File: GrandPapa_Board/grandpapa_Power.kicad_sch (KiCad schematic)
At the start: 0 parts

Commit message: Shameless papa copying pt 1
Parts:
- added C?: 0.1uF, Capacitor_SMD:C_0805_2012Metric_Pad1.18x1.45mm_HandSolder, symbol Device:C
- added F?: 500mA, Fuse:Fuse_0805_2012Metric_Pad1.15x1.40mm_HandSolder, symbol Device:Fuse_Small
- added J? (x3): Conn_01x02_Female, Connector_JST:JST_PH_S2B-PH-K_1x02_P2.00mm_Horizontal, symbol Connector:Conn_01x02_Female
- added J?: Conn_01x03_Female, symbol Connector:Conn_01x03_Female
- added R?: 20mR, Resistor_SMD:R_1206_3216Metric_Pad1.30x1.75mm_HandSolder, symbol Device:R_US
- added TP?: TestPoint, Connector_PinHeader_2.54mm:PinHeader_1x01_P2.54mm_Vertical, symbol Connector:TestPoint
- added U? (x2): LM2594M-5.0, Package_SO:SOIC-8_3.9x4.9mm_P1.27mm, symbol Regulator_Switching:LM2594M-5.0
- added U?: INA180A4QDBVRQ1, Package_TO_SOT_SMD:SOT-23-5_HandSoldering, symbol payload2020_custom:INA180
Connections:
- new net: F?.2, R?.2, U?.3 (IN+)
- new net +12V: U?.7 (VIN), U?.7 (VIN)
- new net +5V: C?.2, U?.5 (VS), U?.8 (OUT), U?.8 (OUT)
- new net +BATT: R?.1, TP?.1, U?.4 (IN-)
- new net BATT_CURR_AMP: U?.1 (VO)
- new net GND: C?.1, J?.1 (Pin_1), U?.2 (GND)
- new net UMB_12V: J?.3 (Pin_3)
- no-connect marks 0 -> 1
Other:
- note added: "100V/V"
- note added: "3 LiPO Cells in series"
- note added: "5V always on for MCU and CAN"
- note added: "5V supply to other boards"
- note added: "9-12V"
- note added: "Battery Connectors"
- note added: "Charger IC **Magic**"
- note added: "Main Power Supplies"
- note added: "Umbilical 5/12V"

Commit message: Add power circuits and some PIC stuff, grandpapa lib
5V buck, 3.3V LDO, load switches, current and voltage sensing, some PIC stuff
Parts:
- removed F?: 500mA, Fuse:Fuse_0805_2012Metric_Pad1.15x1.40mm_HandSolder, symbol Device:Fuse_Small
- removed U? (x2): LM2594M-5.0, Package_SO:SOIC-8_3.9x4.9mm_P1.27mm, symbol Regulator_Switching:LM2594M-5.0
- added C? (x3): 0.1uF, symbol Device:C_Small
- added C?: C_Small, symbol Device:C_Small
- added C? (x3): 4.7uF, symbol Device:C_Small
- added C?: 10nF, symbol Device:C_Small
- added C?: 1uF, symbol Device:C_Small
- added C?: 30uF, symbol Device:C_Polarized_Small_US
- added C?: 2.2uF, symbol Device:C_Small
- added C?: 0.33uF, symbol Device:C_Small
- added C?: 100uF 10V, symbol Device:C_Polarized_Small_US
- added C?: 0.1uF, Capacitor_SMD:C_0805_2012Metric_Pad1.18x1.45mm_HandSolder, symbol Device:C
- added D?: 1N914, Diode_THT:D_DO-35_SOD27_P7.62mm_Horizontal, symbol Diode:1N914
- added D?: 1N5818, Diode_THT:D_DO-41_SOD81_P10.16mm_Horizontal, symbol Diode:1N5818
- added F?: 2A, symbol Device:Fuse
- added L?: 30uH, symbol Device:L_Small
- added R? (x3): 500R, Resistor_SMD:R_1206_3216Metric_Pad1.30x1.75mm_HandSolder, symbol Device:R_US
- added R?: 62mR, Resistor_SMD:R_1206_3216Metric_Pad1.30x1.75mm_HandSolder, symbol Device:R_US
- added R?: 100k, Resistor_SMD:R_0805_2012Metric_Pad1.20x1.40mm_HandSolder, symbol Device:R_Small_US
- added R?: 0, symbol Device:R_Small_US
- added R?: 10k, Resistor_SMD:R_0805_2012Metric_Pad1.20x1.40mm_HandSolder, symbol Device:R_Small_US
- added R?: 15.8k, symbol Device:R_Small_US
- added R?: 4.99k, symbol Device:R_Small_US
- added TP?: TestPoint, symbol Connector:TestPoint
- added TP?: TestPoint, Connector_PinHeader_2.54mm:PinHeader_1x01_P2.54mm_Vertical, symbol Connector:TestPoint
- added U? (x3): FPF2124, symbol grandpapa board:FPF2124
- added U?: LT1576IS8-5#TRPBF, symbol grandpapa board:LT1576IS8-5#TRPBF
- added U?: INA180A4QDBVRQ1, Package_TO_SOT_SMD:SOT-23-5_HandSoldering, symbol payload2020_custom:INA180
- added U?: LD2985BM33R, symbol grandpapa board:LD2985BM33R
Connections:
- net +5V: now also C?.1, C?.1, C?.1, C?.2, R?.2, TP?.1, U?.1 (VIN), U?.1 (VIN), U?.1 (VIN), U?.5 (VS)
- net +BATT: now also C?.1, R?.1, U?.2 (VIN)
- net GND: now also J?.1 (Pin_1), C?.1, C?.2, C?.2, C?.2, C?.2, C?.2, C?.2, C?.2, C?.2, C?.2, C?.2, C?.2, C?.2, D?.2 (A), R?.1, R?.2, R?.2, R?.2, R?.2, U?.2 (GND), U?.2 (GND), U?.2 (GND), U?.2 (GND), U?.2 (GND), U?.4 (GND), U?.8 (~{SHDN/SYNC})
- net RAW_BATT: now reaches R?.2, U?.3 (IN+)
- net RAW_BATT: now also F?.2
- net at J?.1 (Pin_1): now also J?.2 (Pin_2)
- net at J?.2 (Pin_2): now also J?.1 (Pin_1)
- net at J?.2 (Pin_2): now also F?.1
- new net: R?.1, U?.4 (ISET) (x3)
- new net: C?.1, D?.1 (K), U?.3 (BOOST)
- new net: C?.1, D?.2 (A), L?.2, R?.1, R?.2, U?.5 (BIAS)
- new net: C?.2, D?.1 (K), L?.1, U?.1 (VSW)
- new net: C?.1, U?.6 (VC)
- new net: R?.1, R?.2, U?.7 (FB/SENSE)
- new net: C?.1, R?.2, U?.3 (IN+), U?.5 (OUT)
- new net: C?.1, U?.4 (BYP)
- new net +3V3: R?.1, TP?.1, U?.4 (IN-)
- new net 3V3_CURR_AMP: U?.1 (VO)
- new net 5V_ALWAYS_ON: C?.1, U?.1 (IN), U?.3 (INHIB)
- new net 5V_LOGGER: C?.1, U?.5 (VOUT)
- new net 5V_MINISENSOR: C?.1, U?.5 (VOUT)
- new net 5V_STRAIN_GUAGE_AMP: C?.1, U?.5 (VOUT)
- new net LOGGER_PWR_EN: U?.3 (ON)
- new net MINISENSOR_PWR_EN: U?.3 (ON)
- new net STRAIN_GUAGE_AMP_PWR_EN: U?.3 (ON)
- new net V_SENSE: R?.1, R?.2
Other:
- note added: "1.09-1.46V output"
- note added: "12-16V"
- note added: "20mR * 100V/V * Imax = 5V Imax = 2.5A"
- note added: "3.3V LDO ALWAYS ON: PIC SUPPLY VOLTAGE"
- note added: "5V ALWAYS ON BUCK REGULATOR"
- note added: "62mR * 100V/V * Imax = 5V Imax = 0.81A"
- note added: "ALUMINUM CAP"
- note added: "ALWAYS ON"
- note added: "ENABLE AT >1.3V"
- note added: "ILIM = 460/RSET = 460/500R = 0.92A CURRENT LIMIT THROUGH EACH OF THE SWITCHES"
- note added: "IMAX = 1.25A"
- note added: "IMAX = 150mA"
- note added: "INPUT CAP CAN BE BETWEEN 15uF - 50uF"
- note added: "L = 60uH FOR LOADS BETWEEN 0.6A AND 1A"
- note added: "PERIPHERAL BOARD LOAD SWITCHES"
- note added: "TANTALLUM CAP"
- note added: "Voltage Sensing"
- note removed: "5V always on for MCU and CAN"
- note removed: "5V supply to other boards"
- moved on the sheet: C?, R?, TP?, U?

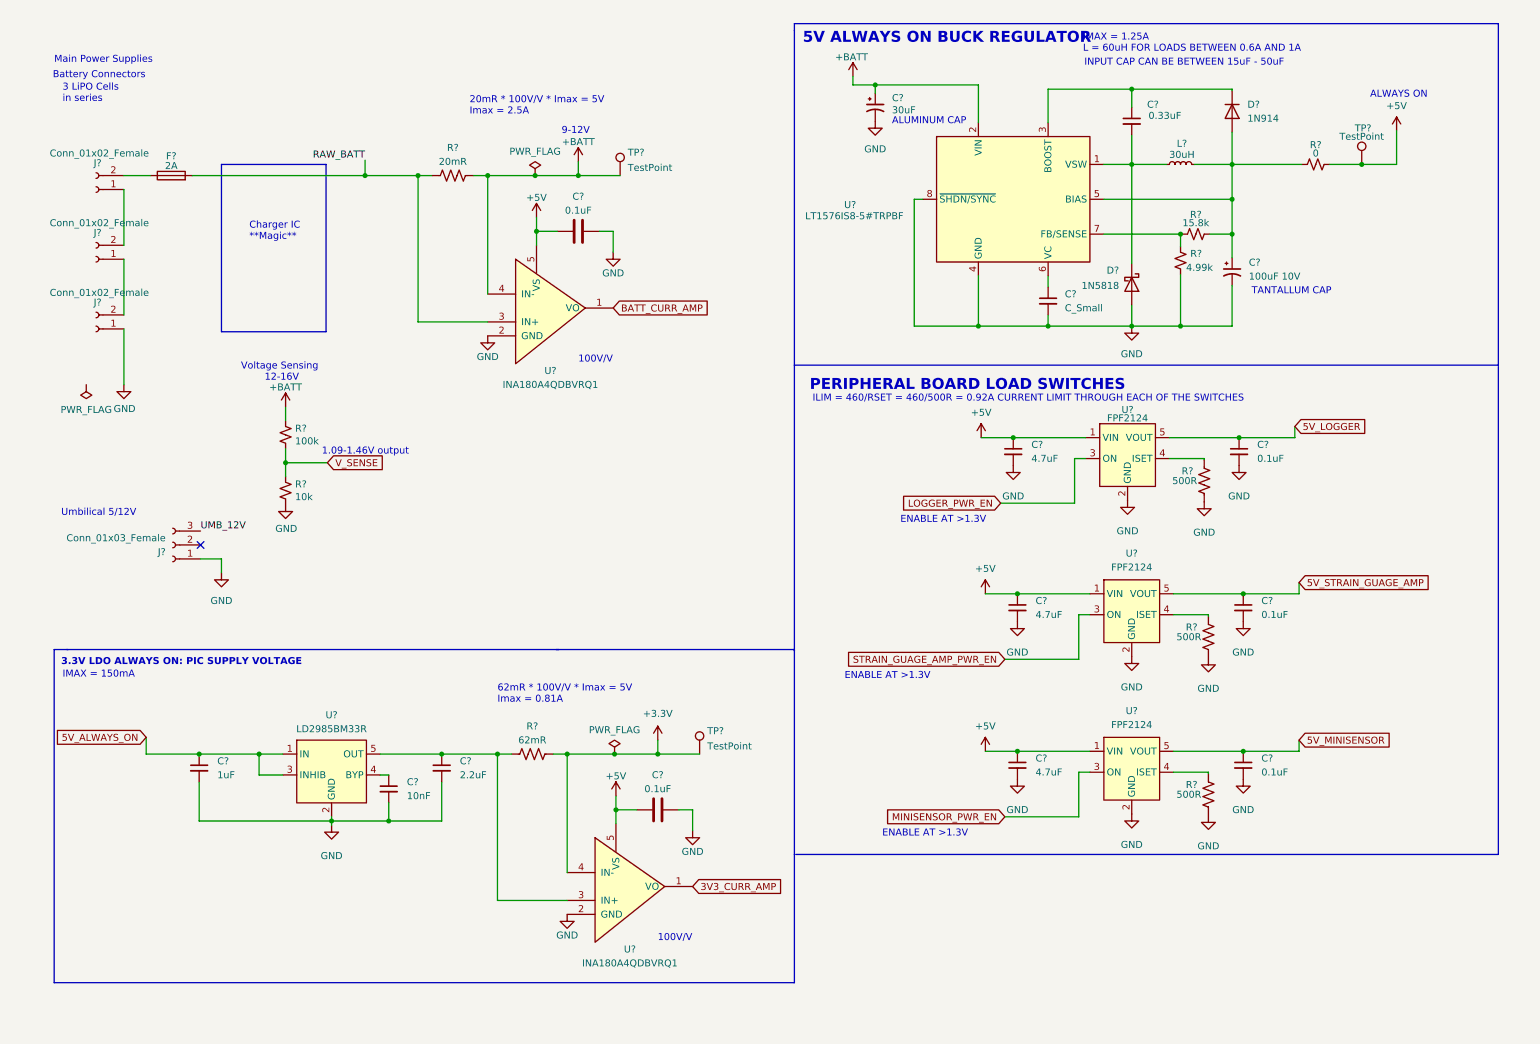
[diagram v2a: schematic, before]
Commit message: Add missing capacitor value, annotate symbols
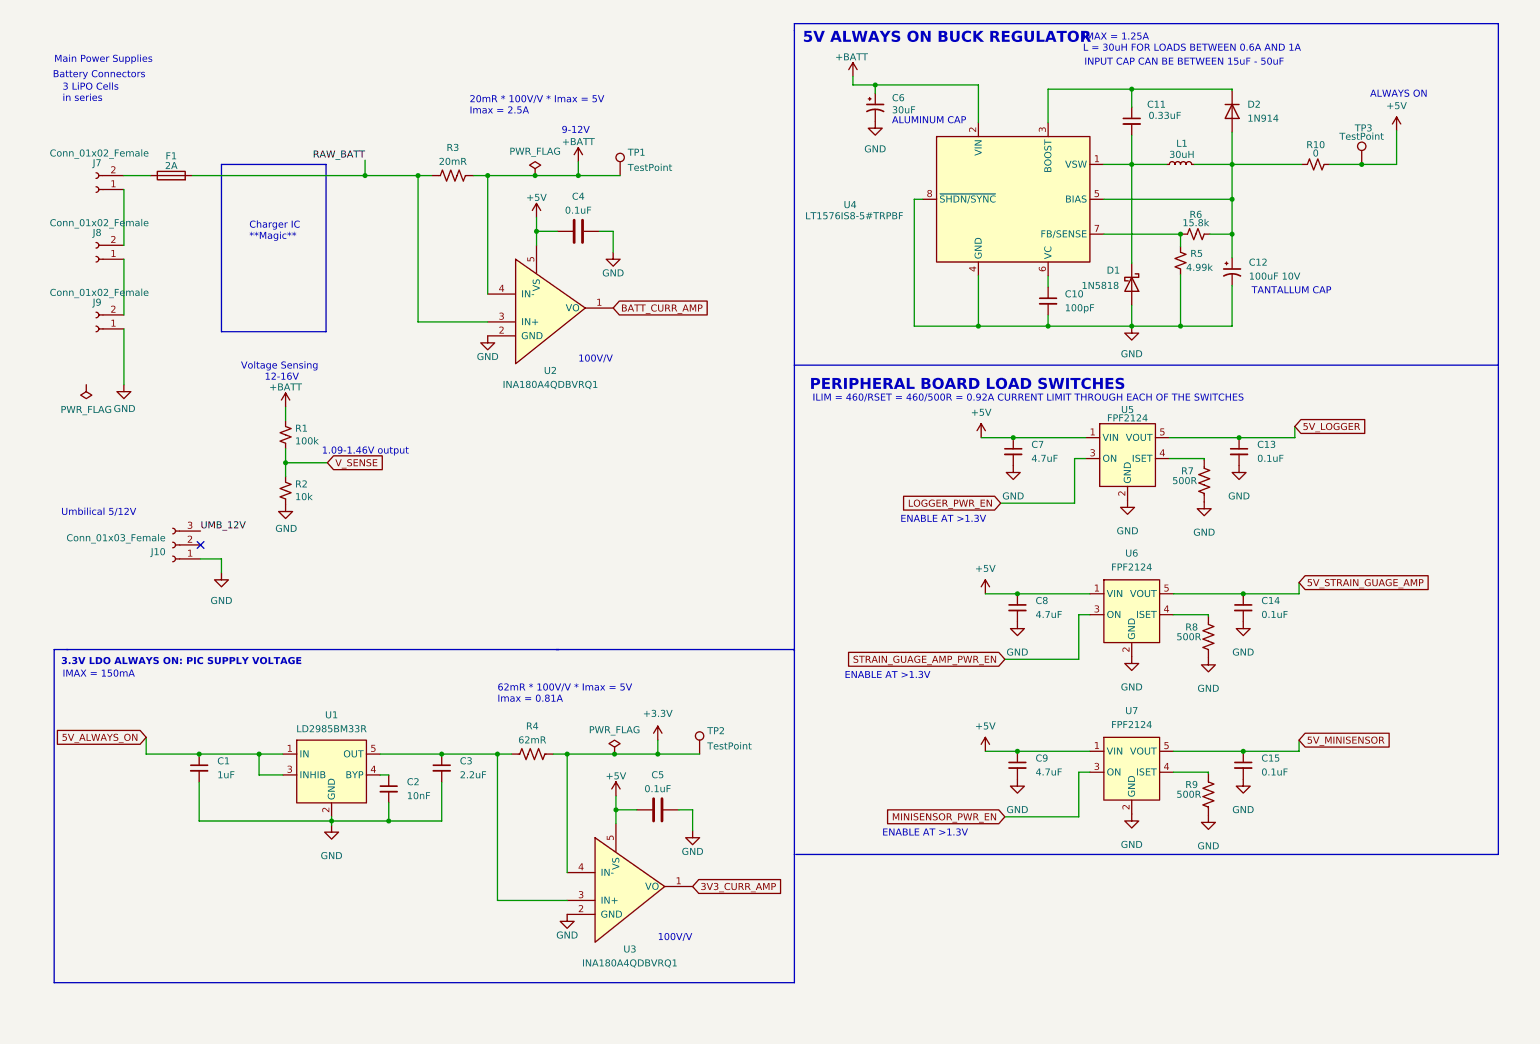
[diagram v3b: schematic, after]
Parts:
- C10: renamed from C?; value C_Small -> 100pF
- gave numbers to parts that had none: 42
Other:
- note added: "L = 30uH FOR LOADS BETWEEN 0.6A AND 1A"
- note removed: "L = 60uH FOR LOADS BETWEEN 0.6A AND 1A"

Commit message: Add motor current sense amp and board output connections
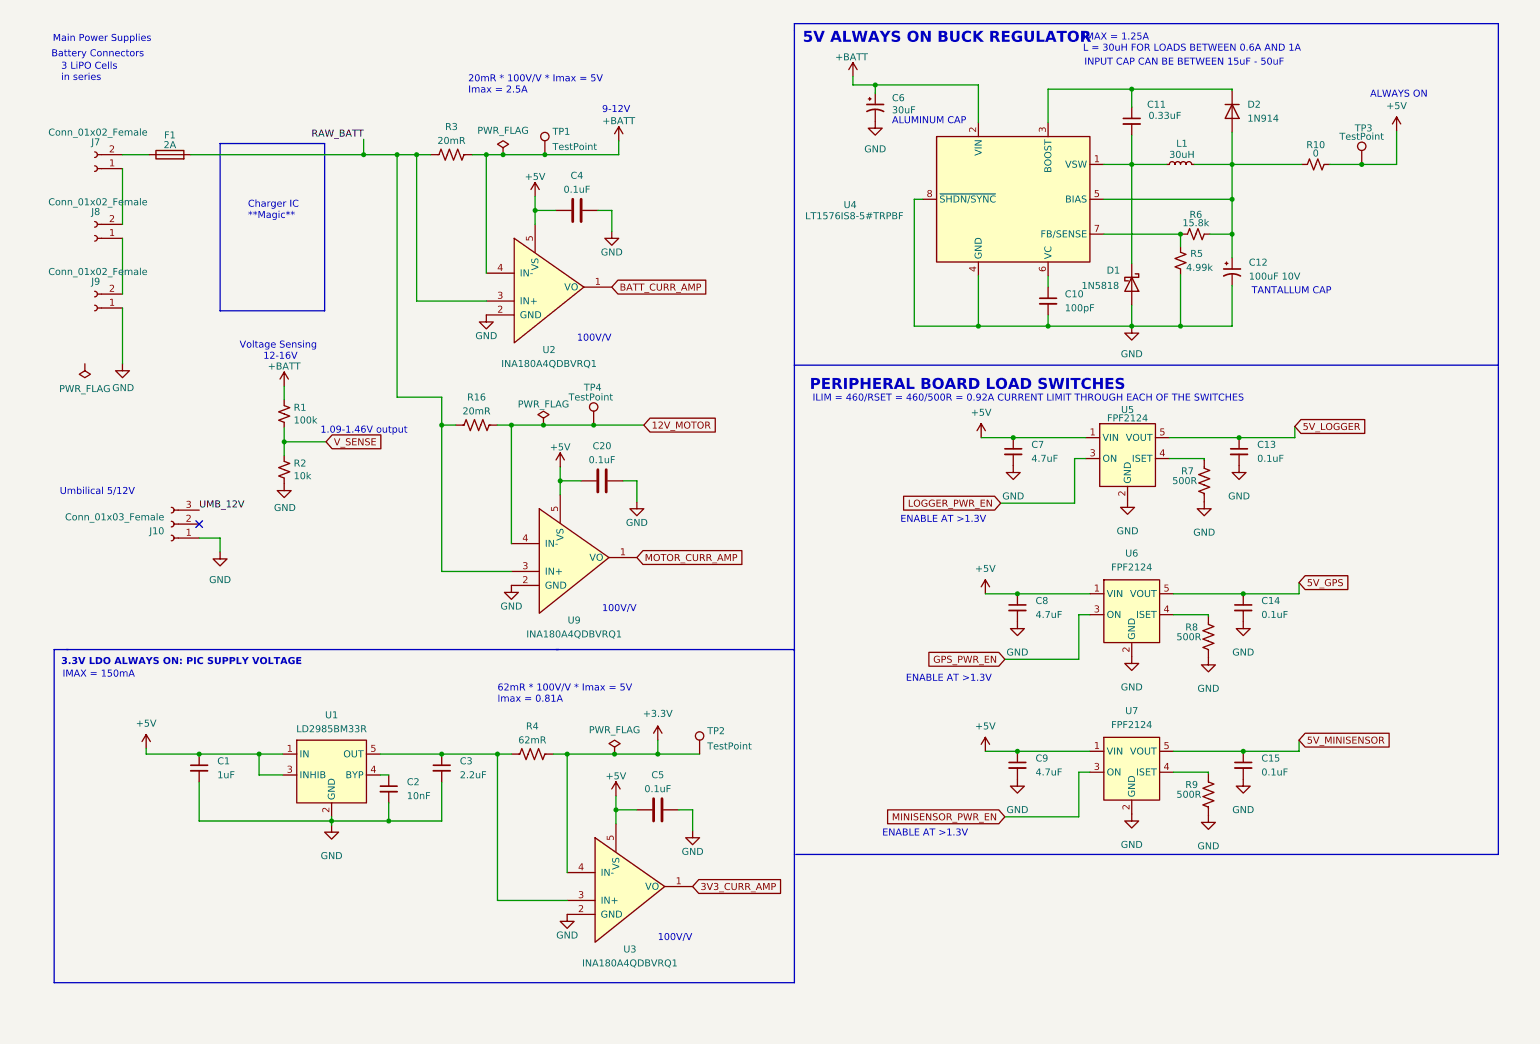
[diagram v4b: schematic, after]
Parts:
- added C20: 0.1uF, Capacitor_SMD:C_0805_2012Metric_Pad1.18x1.45mm_HandSolder, symbol Device:C
- added R16: 20mR, Resistor_SMD:R_1206_3216Metric_Pad1.30x1.75mm_HandSolder, symbol Device:R_US
- added TP4: TestPoint, Connector_PinHeader_2.54mm:PinHeader_1x01_P2.54mm_Vertical, symbol Connector:TestPoint
- added U9: INA180A4QDBVRQ1, Package_TO_SOT_SMD:SOT-23-5_HandSoldering, symbol payload2020_custom:INA180
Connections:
- net 5V_ALWAYS_ON is gone; now on net +5V: C1.1, U1.1 (IN), U1.3 (INHIB)
- net +5V: now also C20.2, U9.5 (VS)
- net GND: now also C20.1, U9.2 (GND)
- net RAW_BATT: now also R16.2, U9.3 (IN+)
- net 5V_STRAIN_GUAGE_AMP renamed 5V_GPS
- net STRAIN_GUAGE_AMP_PWR_EN renamed GPS_PWR_EN
- new net 12V_MOTOR: R16.1, TP4.1, U9.4 (IN-)
- new net MOTOR_CURR_AMP: U9.1 (VO)
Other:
- moved on the sheet: C4, F1, J10, J7, J8, J9, R1, R2, R3, TP1, U2

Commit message: Add INA180 to symbol lib, update 5v switch labels
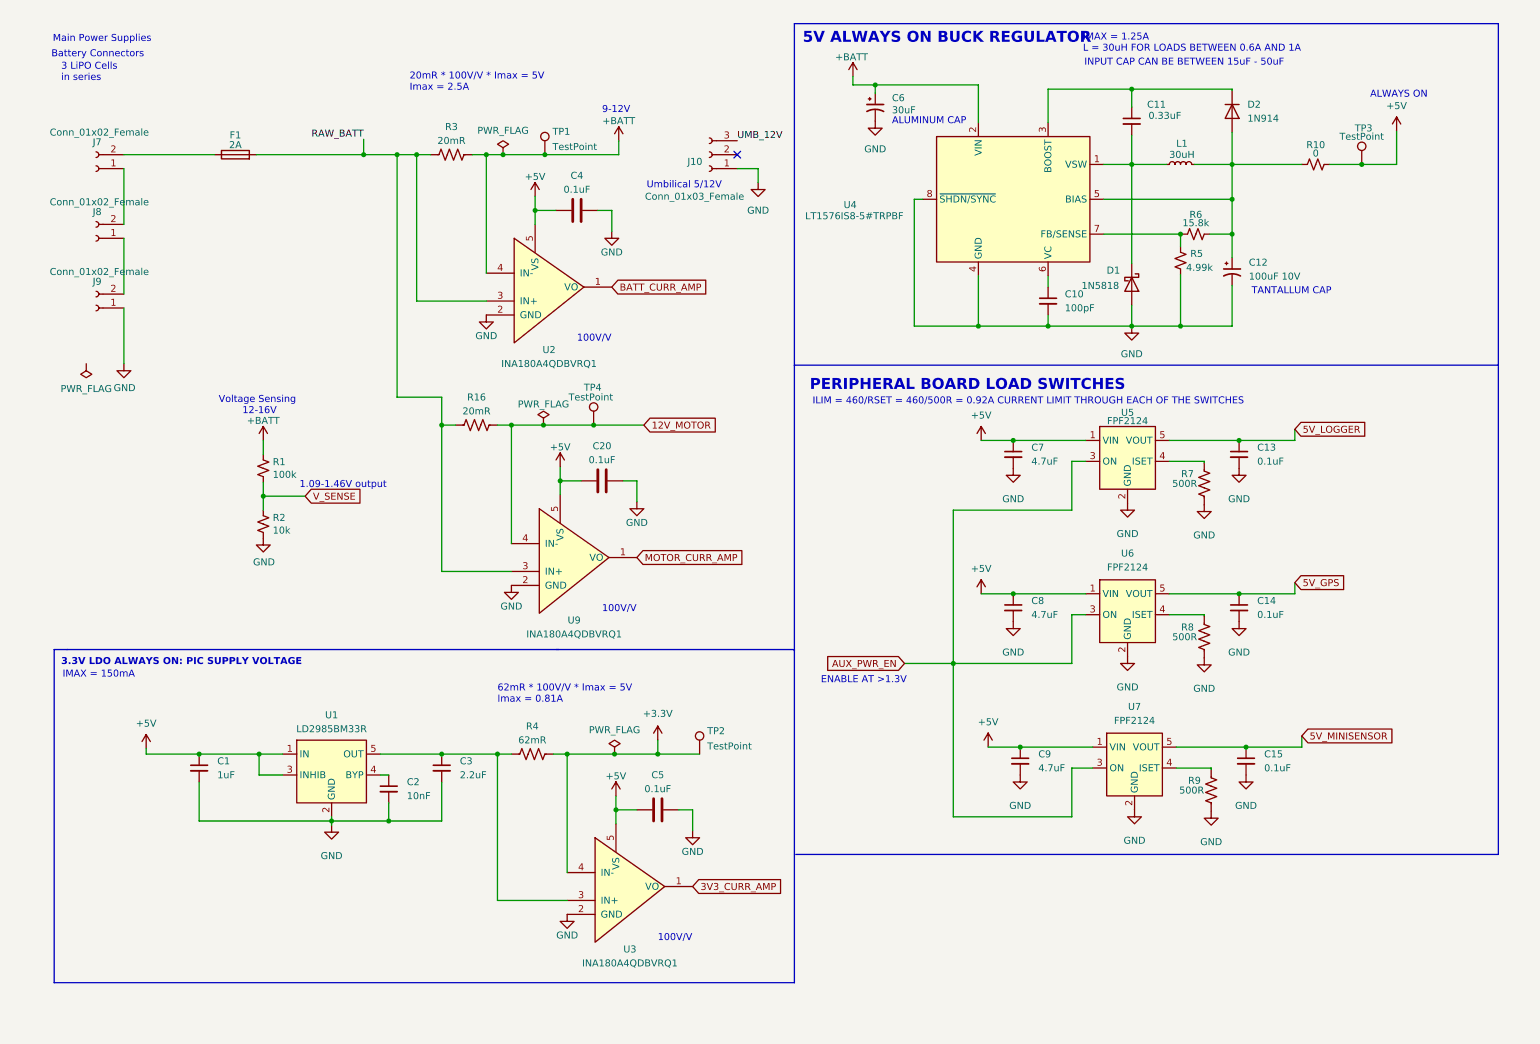
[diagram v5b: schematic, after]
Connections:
- net LOGGER_PWR_EN is gone; now on net AUX_PWR_EN: U5.3 (ON)
- net MINISENSOR_PWR_EN is gone; now on net AUX_PWR_EN: U7.3 (ON)
- net GPS_PWR_EN renamed AUX_PWR_EN
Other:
- note removed: "Charger IC **Magic**"
- moved on the sheet: C13, C14, C15, C7, C8, C9, F1, J10, R1, R2, R7, R8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
